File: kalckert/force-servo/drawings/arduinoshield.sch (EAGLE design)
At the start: 36 parts, among them IC1 MCP604P, IC3 7806T, IC5 MCP604P

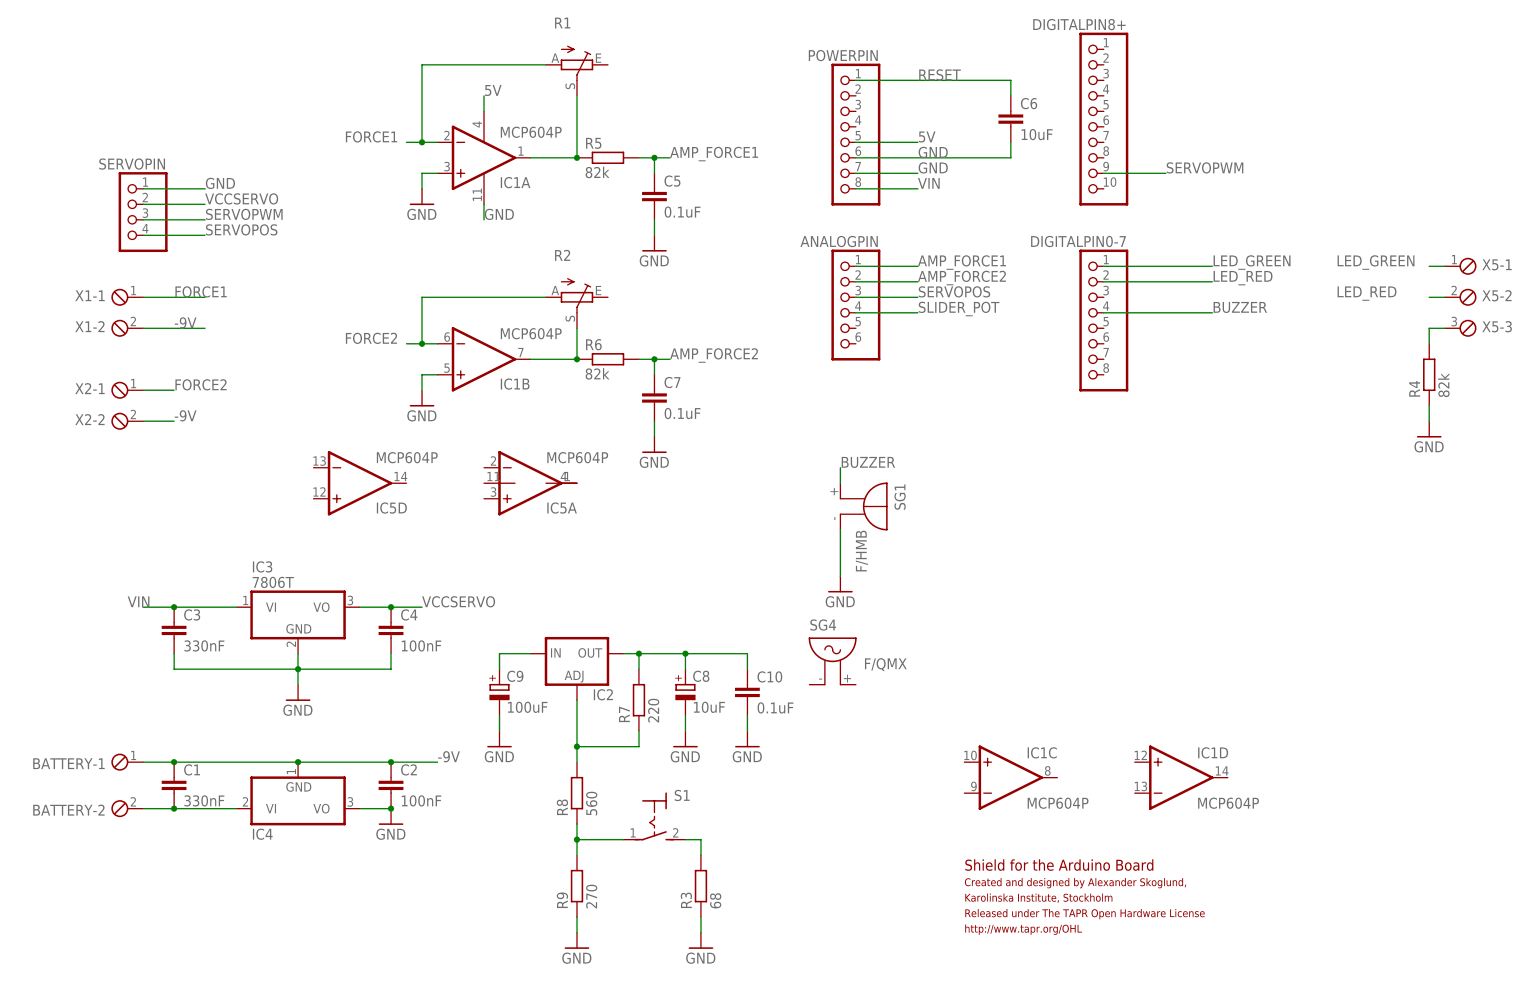
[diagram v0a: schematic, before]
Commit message: Moved tapometer from its own folder to project folder and added drawings and the CERn hardware licence to the drawings.
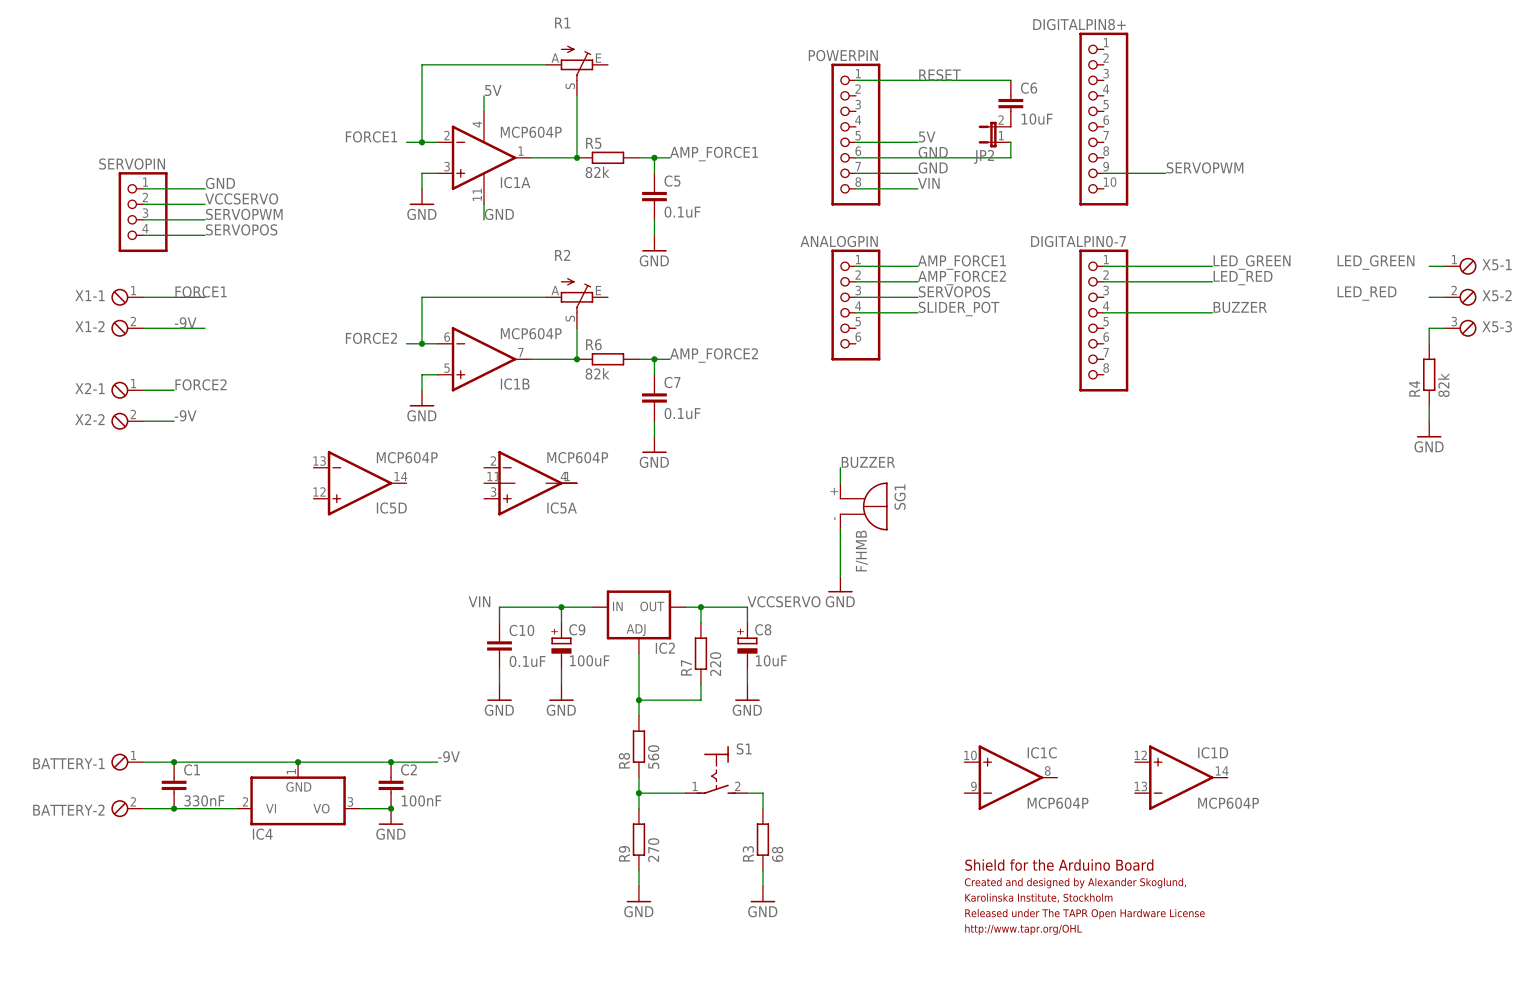
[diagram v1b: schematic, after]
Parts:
- removed C3: 330nF, rcl:C-EU025-025X050
- removed C4: 100nF, rcl:C-EU025-025X050
- removed IC3: 7806T, linear:7806T
- removed SG4: F/QMX, buzzer:F/QMX
- added JP2: (no value), jumper:JP1E
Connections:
- removed net N$14: C9.+, IC2.IN
- removed net N$20: C10.1, C8.+, IC2.OUT, R7.2
- net GND: now also JP2.1; no longer C6.2
- net N$3: now also C6.2, JP2.2; no longer C3.2, C4.2, IC3.GND
- net VCCSERVO: now also C8.+, IC2.OUT, R7.2; no longer C4.1, IC3.VO
- net VIN: now also C10.1, C9.+, IC2.IN; no longer C3.1, IC3.VI
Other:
- moved on the sheet: C10, C6, C8, C9, IC2, R3, R7, R8, R9, S1
